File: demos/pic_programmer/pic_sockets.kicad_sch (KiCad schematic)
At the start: 7 parts, among them P2 SUPP28, P3 SUPP40, U1 24Cxx, U5 PIC_18_PINS, U6 PIC_8_PINS

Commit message: Update demos.
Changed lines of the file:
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@@
-(kicad_sch (version 20210126) (generator eeschema)
+(kicad_sch (version 20210406) (generator eeschema)
   (paper "A4")
   (title_block
@@
       (effects (font (size 1.524 1.524)) hide)
     )
+    (pin "4")
+    (pin "8")
     (pin "1")
     (pin "2")
@@
     (pin "6")
     (pin "7")
-    (pin "4")
-    (pin "8")
   )
   (symbol (lib_id "pic_programmer_schlib:SUPP28") (at 218.44 64.77 0) (unit 1)

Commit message: Demos update
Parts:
- U: renamed from U6; value PIC_8_PINS -> (none); footprint Package_DIP:DIP-8_W7.62mm_Socket_LongPads -> (none)
- U: renamed from U5; value PIC_18_PINS -> (none); footprint Package_DIP:DIP-18_W7.62mm_Socket_LongPads -> (none)
- U: renamed from U1; value 24Cxx -> (none); footprint Package_DIP:DIP-8_W7.62mm_Socket_LongPads -> (none)
- U: renamed from P3; value SUPP40 -> (none); footprint footprints:40tex-Ell600 -> (none)
- U: renamed from C6; value 100nF -> (none); footprint Capacitor_THT:C_Disc_D5.1mm_W3.2mm_P5.00mm -> (none)
- U: renamed from C7; value 100nF -> (none); footprint Capacitor_THT:C_Disc_D5.1mm_W3.2mm_P5.00mm -> (none)
- U: renamed from P2; value SUPP28 -> (none); footprint Package_DIP:DIP-28_W7.62mm_Socket_LongPads -> (none)

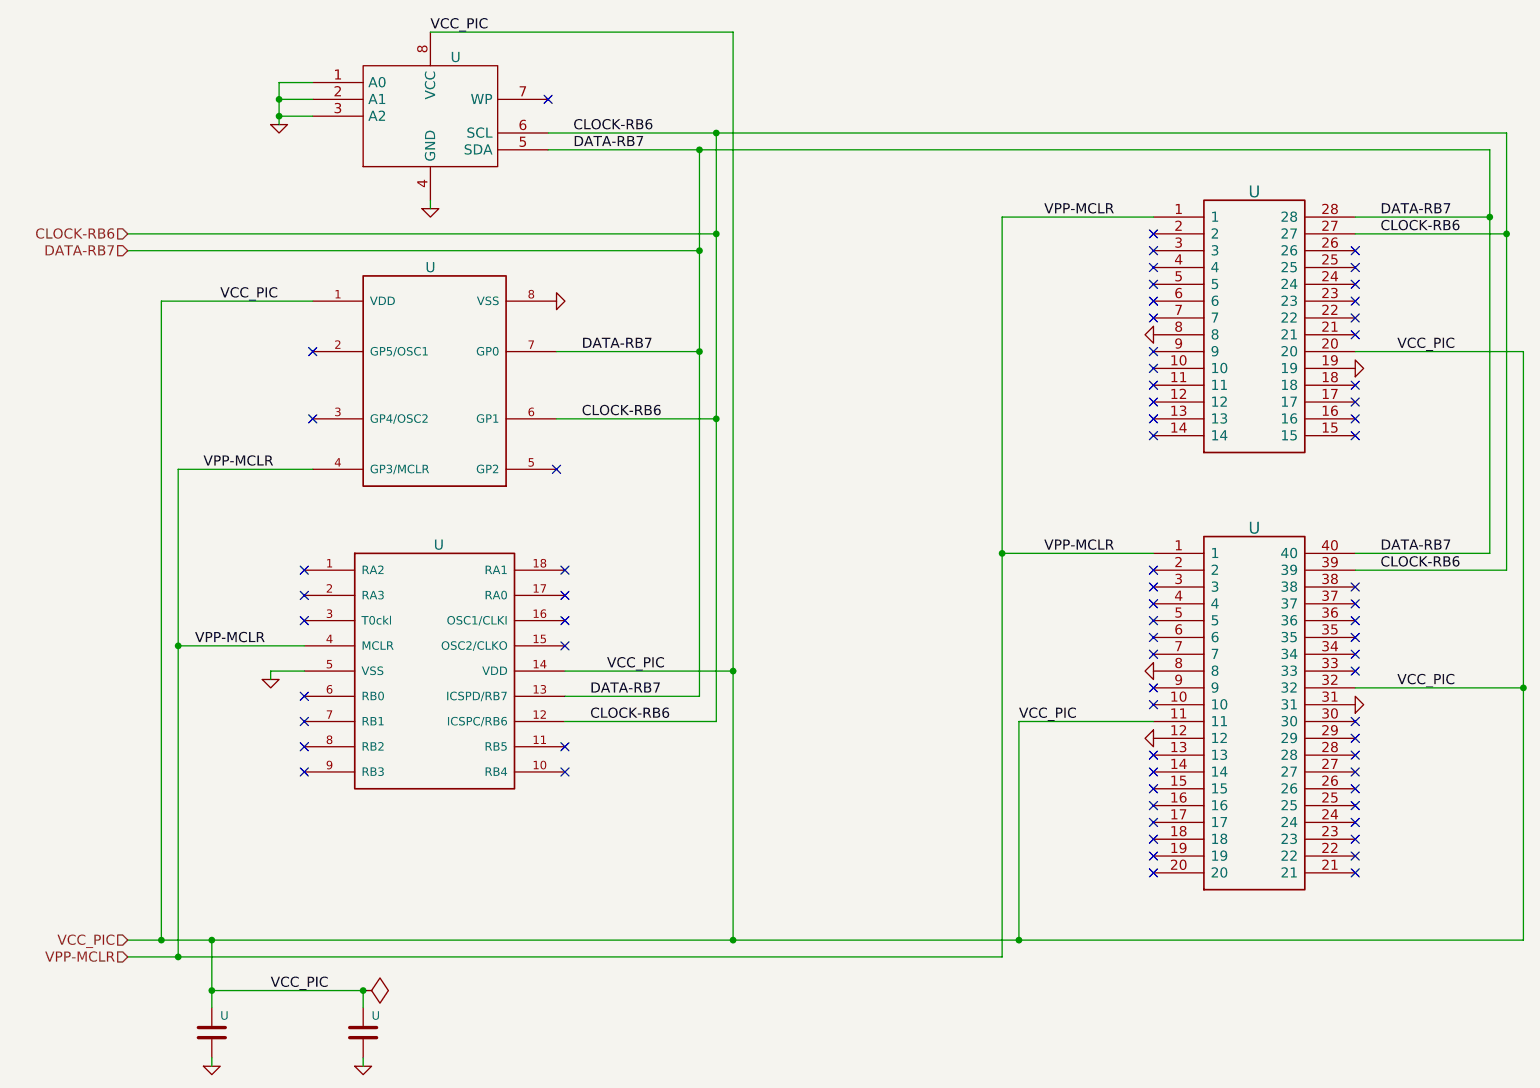
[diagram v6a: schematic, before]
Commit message: Update demos using latest file formats.
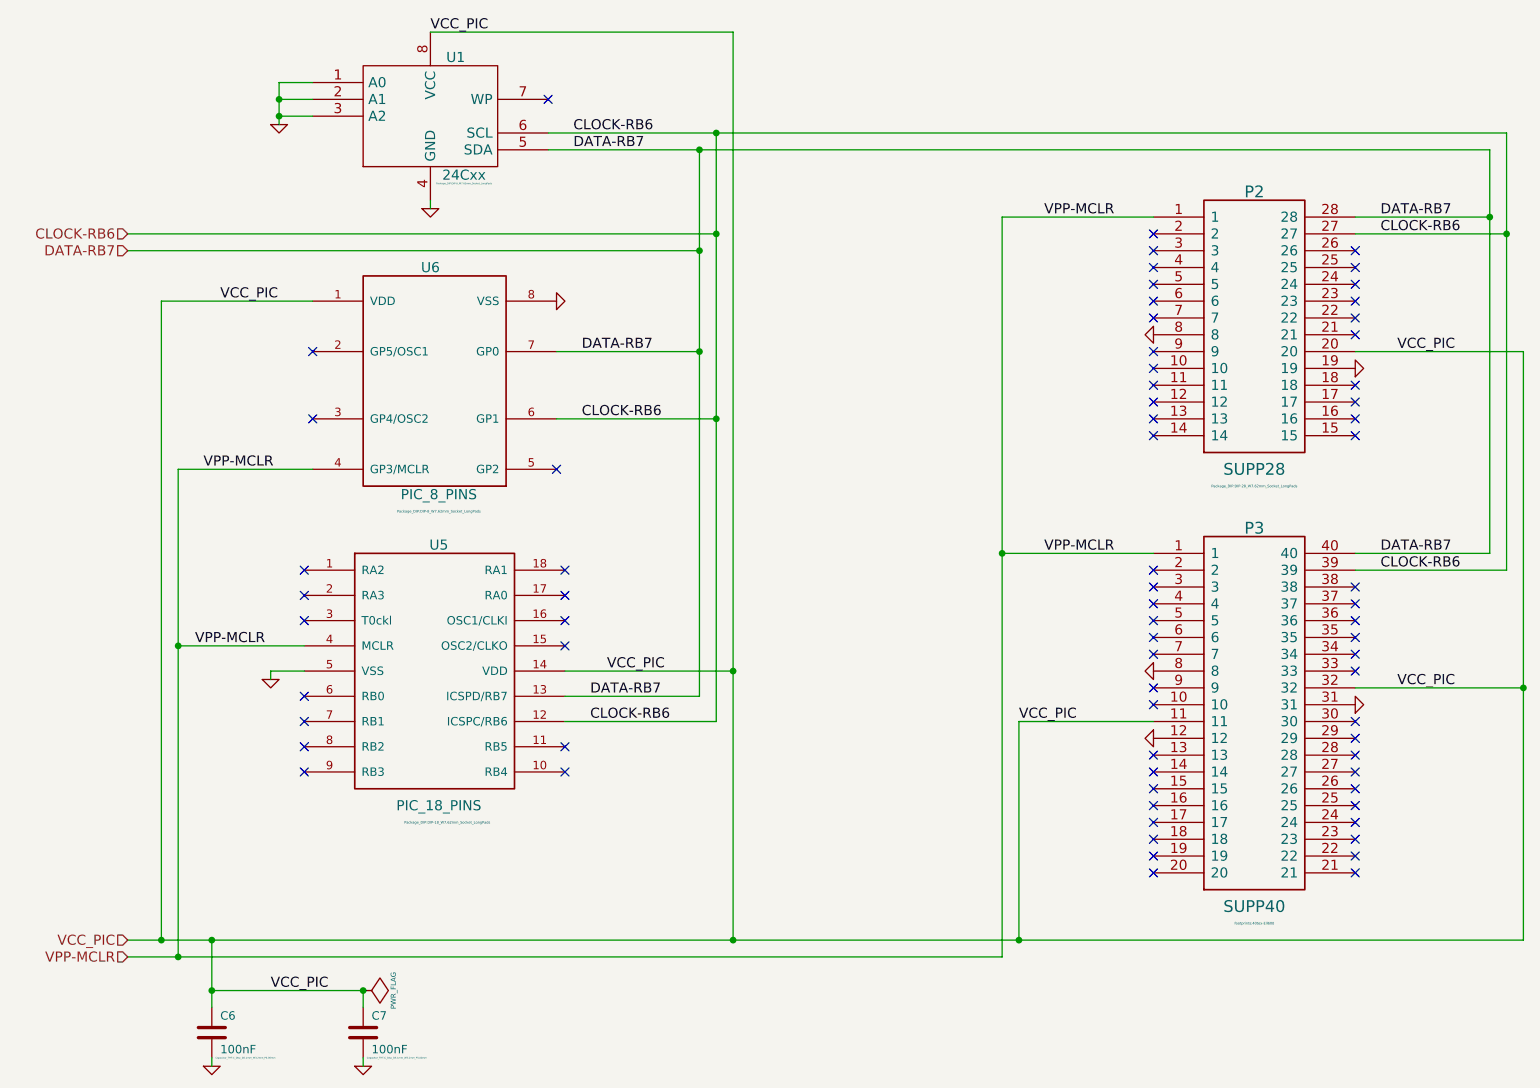
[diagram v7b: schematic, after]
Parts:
- C6, C7: renamed from U; value (none) -> 100nF; footprint (none) -> Capacitor_THT:C_Disc_D5.1mm_W3.2mm_P5.00mm
- P2: renamed from U; value (none) -> SUPP28; footprint (none) -> Package_DIP:DIP-28_W7.62mm_Socket_LongPads
- P3: renamed from U; value (none) -> SUPP40; footprint (none) -> footprints:40tex-Ell600
- U1: renamed from U; value (none) -> 24Cxx; footprint (none) -> Package_DIP:DIP-8_W7.62mm_Socket_LongPads
- U5: renamed from U; value (none) -> PIC_18_PINS; footprint (none) -> Package_DIP:DIP-18_W7.62mm_Socket_LongPads
- U6: renamed from U; value (none) -> PIC_8_PINS; footprint (none) -> Package_DIP:DIP-8_W7.62mm_Socket_LongPads
